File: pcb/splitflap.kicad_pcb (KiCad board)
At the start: 2 copper layers, 100 x 100 mm, 88 parts, among them J1 Motor D, J10 Hall C, J11 Hall B, J12 I2C, J2 Motor C, J3 Motor B, J4 Motor A, J5 BarrelJack Vertical, J6 USB_C_Receptacle_USB2.0_16P, J7 BarrelJack Horizontal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

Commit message: Add logo to the PCB
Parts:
- added G***: LOGO, LOGO, F.Cu at (109.8, 103.1)
- added G***: LOGO, LOGO, B.Cu at (143.4, 96.2)
- moved OSHW1 78.5 mm to (109.8, 71.8)
- moved R6 0.40 mm to (135.4, 145.0)

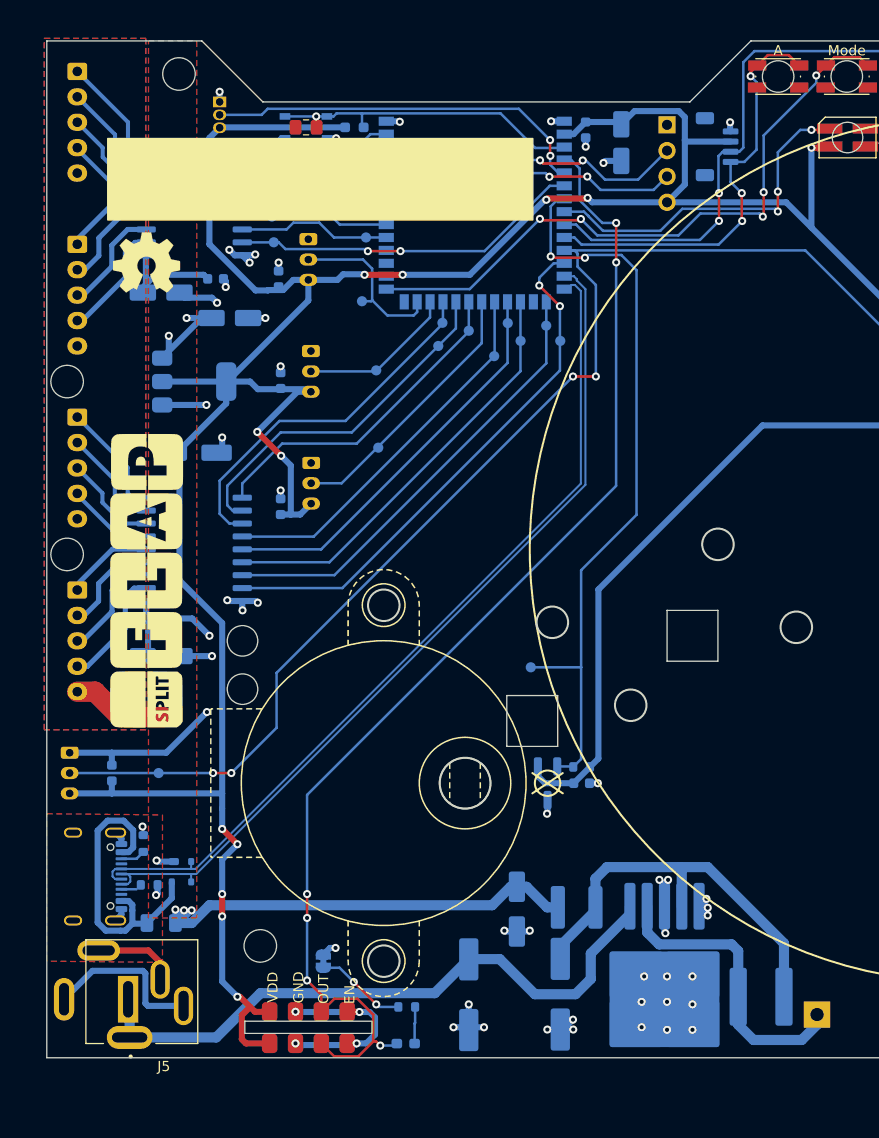
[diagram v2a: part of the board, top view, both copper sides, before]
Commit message: Silkscreen: Logo / Date / Commit Placeholder / Labels / PCB Way logo
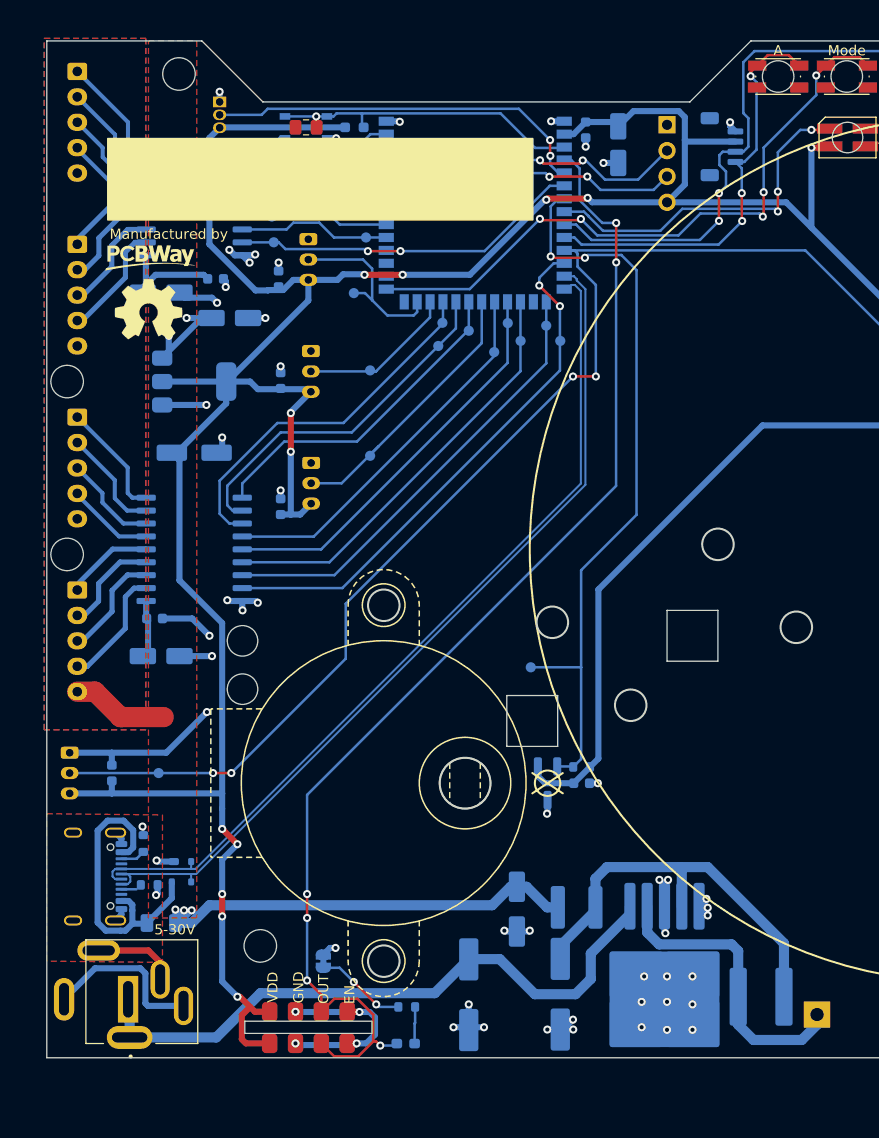
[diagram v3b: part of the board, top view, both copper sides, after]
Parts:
- G***: value LOGO -> Manufactured by
- J8, U5: value Hall A1 -> Hall Internal
- U9: value Hall A2 -> Hall Internal2
- moved G*** 32.1 mm to (110.2, 71.0), turned to 0 degrees
- moved OSHW1 4.60 mm to (110.0, 76.4)
- moved TP21 1.13 mm to (130.2, 74.8)
- moved TP19 1.13 mm to (131.8, 90.8)
- moved TP20 0.60 mm to (131.8, 82.4)
- moved J12 0.47 mm to (166.4, 60.4)
- moved TP8 0.40 mm to (144.0, 80.6)
- moved C16 0.36 mm to (156.2, 60.2)
- moved TP16 0.12 mm to (129.8, 60.9)
- turned G*** to -90 degrees
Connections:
- net /HALL_A2 renamed /HALL_INTERNAL2
- J8 pad 2: /HALL_A1 -> /HALL_INTERNAL
- R7 pad 2: /HALL_A1 -> /HALL_Internal
- TP17 pad 1: /HALL_A1 -> /HALL_INTERNAL
- U4 pad 11: /HALL_A1 -> /HALL_INTERNAL
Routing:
- net /HALL_A1: track 133.7 -> 0.00 mm, vias 6 -> 0
- net (no net): track 0.00 -> 133.7 mm
- net +3V3: track 360.5 -> 357.6 mm
- net /SWB_SDA: track 55.2 -> 56.3 mm
- net /HALL_D: track 17.0 -> 18.0 mm
- net /HALL_B: track 26.8 -> 27.8 mm
- net /SWA_SCL: track 41.8 -> 41.2 mm
- net /HALL_C: track 15.6 -> 16.1 mm
- net /HALL_INTERNAL: vias 0 -> 6
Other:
- board text added: "- < > +"
- board text added: "v2.0 @abcdef Designed in Switzerland Besmer Labs 24.03.2025 github.com/besi/split-flap-clock"

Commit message: Add Pinout
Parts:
- added G***: LOGO, LOGO, F.Cu at (114.2, 88.4)
- moved OSHW1 1.51 mm to (111.5, 76.6)
- moved G*** 0.73 mm to (110.9, 71.2)
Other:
- outline, holes or cut-outs redrawn
- board text added: "#279"
- board text added: "Pinout - Hall A: 10 9 3 8 - 18 (7) B: 13 14 21 11 - 12 C: 40 39 38 6 - 47 D: 1 2 42 41 - 48 DCF77: 4 SDA / SWB: 16 SCL / SWA: 17 Mode: 0 Neopixel: 15 Temp: 5"

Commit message: Fix HALL_INTERNAL label
The layout is not affected
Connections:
- R7 pad 2: /HALL_Internal -> /HALL_INTERNAL
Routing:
- net /HALL_INTERNAL: track 0.00 -> 133.7 mm
- net (no net): track 133.7 -> 0.00 mm
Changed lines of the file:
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@@
 	(net 67 "VBUS")
 	(net 68 "Net-(U5-OUTPUT)")
-	(net 69 "/HALL_Internal")
-	(net 70 "/HALL_INTERNAL")
+	(net 69 "/HALL_INTERNAL")
 	(footprint "Button_Switch_SMD:SW_Push_1P1T_NO_Vertical_Wuerth_434133025816"
 		(layer "F.Cu")
@@
 			(layers "*.Cu" "*.Mask")
 			(remove_unused_layers no)
-			(net 70 "/HALL_INTERNAL")
+			(net 69 "/HALL_INTERNAL")
 			(pinfunction "Pin_2")
 			(pintype "passive")
@@
 			(size 1.5 0.9)
 			(layers "B.Cu" "B.Paste" "B.Mask")
-			(net 70 "/HALL_INTERNAL")
+			(net 69 "/HALL_INTERNAL")
 			(pinfunction "IO18")
 			(pintype "bidirectional")
@@
 			(size 1 1)
 			(layers "B.Cu" "B.Mask")
-			(net 70 "/HALL_INTERNAL")
+			(net 69 "/HALL_INTERNAL")
 			(pinfunction "1")
 			(pintype "passive")
@@
 			(layers "B.Cu" "B.Paste" "B.Mask")
 			(roundrect_rratio 0.25)
-			(net 69 "/HALL_Internal")
+			(net 69 "/HALL_INTERNAL")
 			(pintype "passive")
 		)
@@
 	)
 	(segment
-		(start 151.749994 83)
-		(end 154 83)
-		(width 0.25)
-		(layer "F.Cu")
-		(net 0)
-	)
-	(segment
-		(start 189.9 83.749998)
-		(end 188.1 83.749998)
-		(width 0.25)
-		(layer "F.Cu")
-		(net 0)
-	)
-	(segment
-		(start 118.15 122)
-		(end 116.35 122)
-		(width 0.25)
-		(layer "F.Cu")
-		(net 0)
-	)
-	(segment
-		(start 174.6 70.6)
-		(end 150.89 70.6)
-		(width 0.25)
-		(layer "B.Cu")
-		(net 0)
-	)
-	(segment
-		(start 129.4 105.349994)
-		(end 151.749994 83)
-		(width 0.25)
-		(layer "B.Cu")
-		(net 0)
-	)
-	(segment
-		(start 116.35 122)
-		(end 102.25 122)
-		(width 0.25)
-		(layer "B.Cu")
-		(net 0)
-	)
-	(segment
-		(start 187.75 83.75)
-		(end 174.6 70.6)
-		(width 0.25)
-		(layer "B.Cu")
-		(net 0)
-	)
-	(segment
-		(start 192.6 85.2)
-		(end 192.6 85.775)
-		(width 0.25)
-		(layer "B.Cu")
-		(net 0)
-	)
-	(segment
-		(start 189.851578 83.750004)
-		(end 189.899994 83.750004)
-		(width 0.25)
-		(layer "B.Cu")
-		(net 0)
-	)
-	(segment
-		(start 154 83)
-		(end 154 74)
-		(width 0.25)
-		(layer "B.Cu")
-		(net 0)
-	)
-	(segment
-		(start 191.149998 83.749998)
-		(end 192.6 85.2)
-		(width 0.25)
-		(layer "B.Cu")
-		(net 0)
-	)
-	(segment
-		(start 188.1 83.749998)
-		(end 188.099998 83.75)
-		(width 0.25)
-		(layer "B.Cu")
-		(net 0)
-	)
-	(segment
-		(start 189.899994 83.750004)
-		(end 189.9 83.749998)
-		(width 0.25)
-		(layer "B.Cu")
-		(net 0)
-	)
-	(segment
-		(start 188.099998 83.75)
-		(end 187.75 83.75)
-		(width 0.25)
-		(layer "B.Cu")
-		(net 0)
-	)
-	(segment
-		(start 189.9 83.749998)
-		(end 191.149998 83.749998)
-		(width 0.25)
-		(layer "B.Cu")
-		(net 0)
-	)
-	(segment
-		(start 129.4 110.75)
-		(end 129.4 105.349994)
-		(width 0.25)
-		(layer "B.Cu")
-		(net 0)
-	)
-	(segment
-		(start 151.89 70.6)
-		(end 150.89 70.6)
-		(width 0.25)
-		(layer "B.Cu")
-		(net 0)
-	)
-	(segment
-		(start 154 74)
-		(end 152.2 72.2)
-		(width 0.25)
-		(layer "B.Cu")
-		(net 0)
-	)
-	(segment
-		(start 118.15 122)
-		(end 129.4 110.75)
-		(width 0.25)
-		(layer "B.Cu")
-		(net 0)
-	)
-	(segment
-		(start 152.2 70.91)
-		(end 151.89 70.6)
-		(width 0.25)
-		(layer "B.Cu")
-		(net 0)
-	)
-	(segment
-		(start 152.2 72.2)
-		(end 152.2 70.91)
-		(width 0.25)
-		(layer "B.Cu")
-		(net 0)
-	)
-	(segment
 		(start 107.25 116.5)
 		(end 111.5 116.5)
@@
 		(net 68)
 	)
+	(segment
+		(start 151.749994 83)
+		(end 154 83)
+		(width 0.25)
+		(layer "F.Cu")
+		(net 69)
+	)
+	(segment
+		(start 189.9 83.749998)
+		(end 188.1 83.749998)
+		(width 0.25)
+		(layer "F.Cu")
+		(net 69)
+	)
+	(segment
+		(start 118.15 122)
+		(end 116.35 122)
+		(width 0.25)
+		(layer "F.Cu")
+		(net 69)
+	)
 	(via
 		(at 118.15 122)
@@
 		(drill 0.4)
 		(layers "F.Cu" "B.Cu")
-		(net 70)
+		(net 69)
 	)
 	(via
@@
 		(drill 0.4)
 		(layers "F.Cu" "B.Cu")
-		(net 70)
+		(net 69)
 	)
 	(via
@@
 		(drill 0.4)
 		(layers "F.Cu" "B.Cu")
-		(net 70)
+		(net 69)
 	)
 	(via
@@
 		(drill 0.4)
 		(layers "F.Cu" "B.Cu")
-		(net 70)
+		(net 69)
 	)
 	(via
@@
 		(drill 0.4)
 		(layers "F.Cu" "B.Cu")
-		(net 70)
+		(net 69)
 	)
 	(via
@@
 		(drill 0.4)
 		(layers "F.Cu" "B.Cu")
-		(net 70)
+		(net 69)
+	)
+	(segment
+		(start 174.6 70.6)
+		(end 150.89 70.6)
+		(width 0.25)
+		(layer "B.Cu")
+		(net 69)
+	)
+	(segment
+		(start 129.4 105.349994)
+		(end 151.749994 83)
+		(width 0.25)
+		(layer "B.Cu")
+		(net 69)
+	)
+	(segment
+		(start 116.35 122)
+		(end 102.25 122)
+		(width 0.25)
+		(layer "B.Cu")
+		(net 69)
+	)
+	(segment
+		(start 187.75 83.75)
+		(end 174.6 70.6)
+		(width 0.25)
+		(layer "B.Cu")
+		(net 69)
+	)
+	(segment
+		(start 192.6 85.2)
+		(end 192.6 85.775)
+		(width 0.25)
+		(layer "B.Cu")
+		(net 69)
+	)
+	(segment
+		(start 189.851578 83.750004)
+		(end 189.899994 83.750004)
+		(width 0.25)
+		(layer "B.Cu")
+		(net 69)
+	)
+	(segment
+		(start 154 83)
+		(end 154 74)
+		(width 0.25)
+		(layer "B.Cu")
+		(net 69)
+	)
+	(segment
+		(start 191.149998 83.749998)
+		(end 192.6 85.2)
+		(width 0.25)
+		(layer "B.Cu")
+		(net 69)
+	)
+	(segment
+		(start 188.1 83.749998)
+		(end 188.099998 83.75)
+		(width 0.25)
+		(layer "B.Cu")
+		(net 69)
+	)
+	(segment
+		(start 189.899994 83.750004)
+		(end 189.9 83.749998)
+		(width 0.25)
+		(layer "B.Cu")
+		(net 69)
+	)
+	(segment
+		(start 188.099998 83.75)
+		(end 187.75 83.75)
+		(width 0.25)
+		(layer "B.Cu")
+		(net 69)
+	)
+	(segment
+		(start 189.9 83.749998)
+		(end 191.149998 83.749998)
+		(width 0.25)
+		(layer "B.Cu")
+		(net 69)
+	)
+	(segment
+		(start 129.4 110.75)
+		(end 129.4 105.349994)
+		(width 0.25)
+		(layer "B.Cu")
+		(net 69)
+	)
+	(segment
+		(start 151.89 70.6)
+		(end 150.89 70.6)
+		(width 0.25)
+		(layer "B.Cu")
+		(net 69)
+	)
+	(segment
+		(start 154 74)
+		(end 152.2 72.2)
+		(width 0.25)
+		(layer "B.Cu")
+		(net 69)
+	)
+	(segment
+		(start 118.15 122)
+		(end 129.4 110.75)
+		(width 0.25)
+		(layer "B.Cu")
+		(net 69)
+	)
+	(segment
+		(start 152.2 70.91)
+		(end 151.89 70.6)
+		(width 0.25)
+		(layer "B.Cu")
+		(net 69)
+	)
+	(segment
+		(start 152.2 72.2)
+		(end 152.2 70.91)
+		(width 0.25)
+		(layer "B.Cu")
+		(net 69)
 	)
 	(zone

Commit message: Cleanup schematics
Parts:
- J6: value USB_C_Receptacle_USB2.0_16P -> USB-C Plug
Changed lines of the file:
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@@
 			)
 		)
-		(property "Value" "USB_C_Receptacle_USB2.0_16P"
+		(property "Value" "USB-C Plug"
 			(at 0 -5 -90)
 			(unlocked yes)

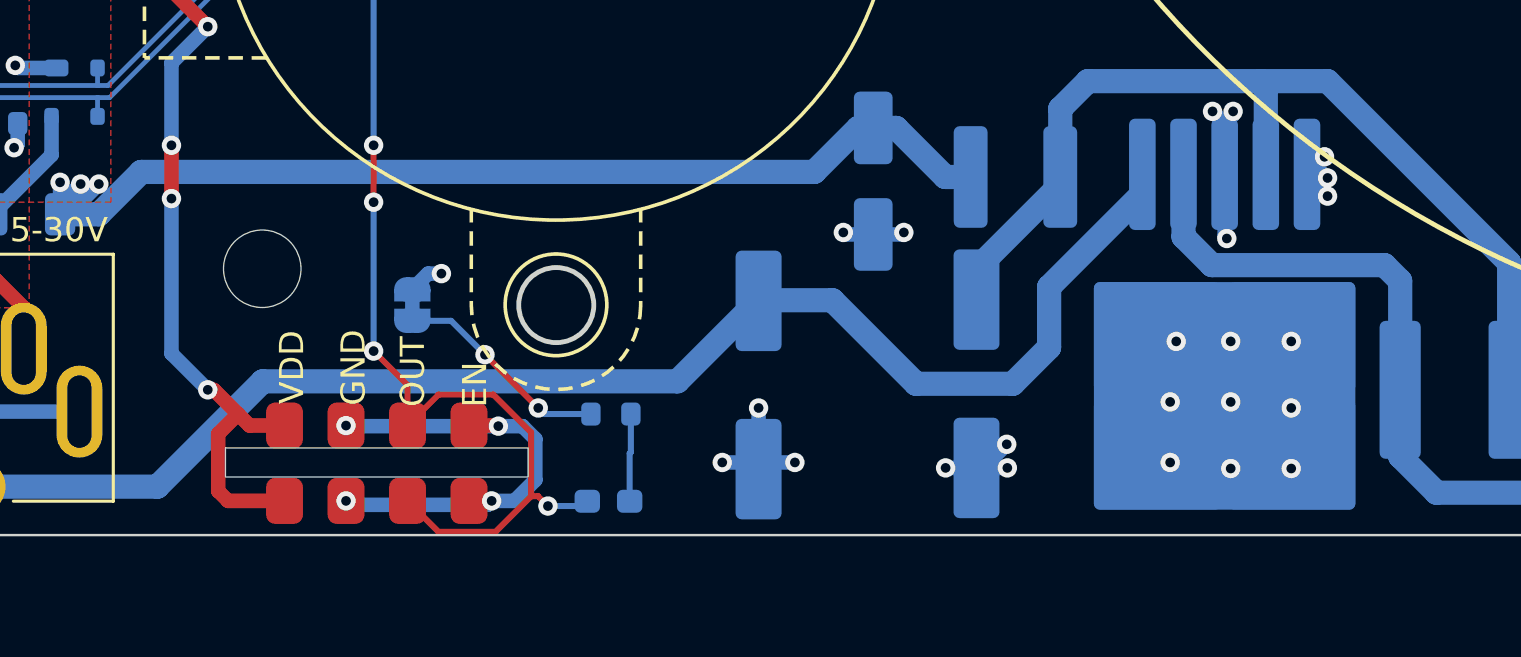
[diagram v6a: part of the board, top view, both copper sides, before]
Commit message: Move vias out of the pads
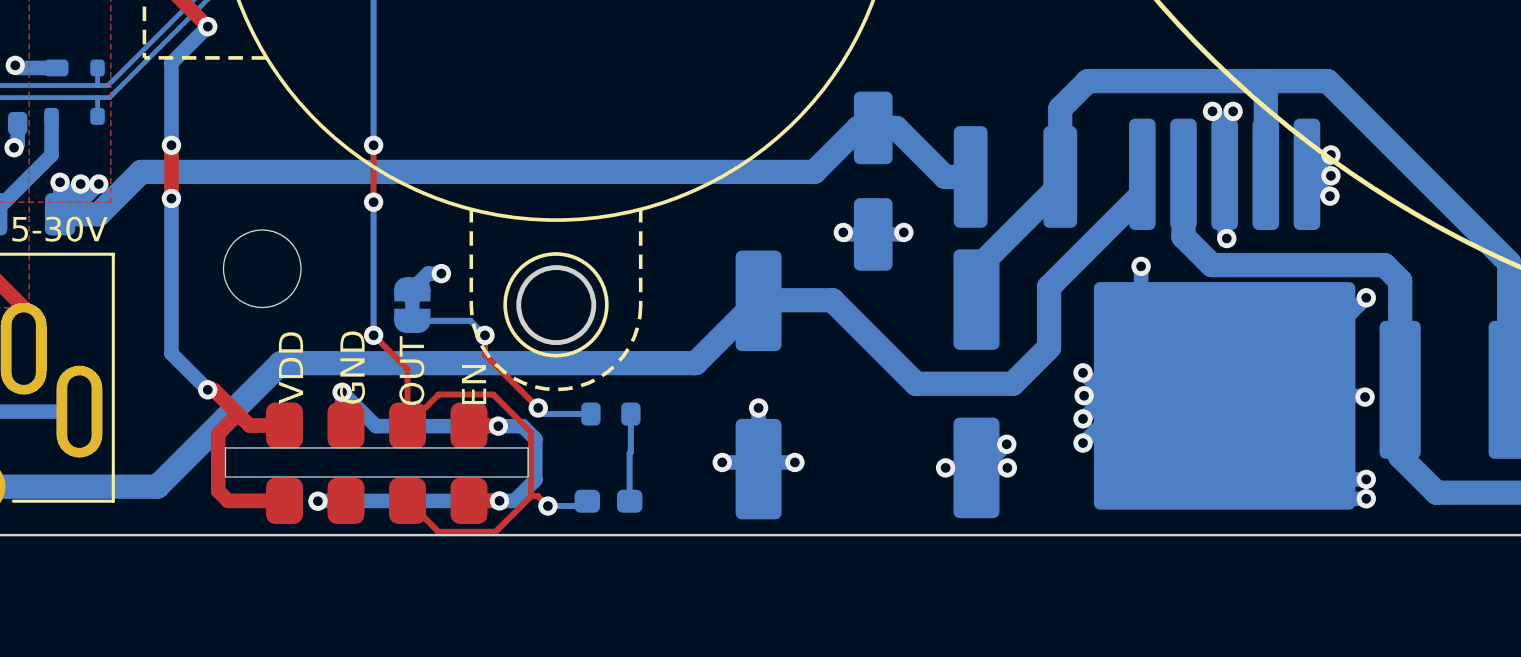
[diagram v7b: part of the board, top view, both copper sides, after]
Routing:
- net GND: track 121.4 -> 180.5 mm

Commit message: Correlate footprints according to the feedback from the Fab-house
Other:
- board text added: "v2.0 @3d2c2404 Designed in Switzerland Besmer Labs 25.03.2025 github.com/besi/split-flap-clock"
- board text removed: "v2.0 @abcdef Designed in Switzerland Besmer Labs 24.03.2025 github.com/besi/split-flap-clock"
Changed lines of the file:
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@@
 			)
 		)
-		(property "MPN" "CP-060A-ND"
+		(property "MPN" "PJ-060A"
 			(at 0 0 180)
 			(unlocked yes)
@@
 		)
 		(model "${KICAD8_3DMODEL_DIR}/Inductor_SMD.3dshapes/L_APV_ANR5045.wrl"
+			(hide yes)
 			(offset
 				(xyz 0 0 0)
@@
 			)
 		)
+		(model "${KIPRJMOD}/lib/TYS5040220M-10.step"
+			(offset
+				(xyz 0 3 0)
+			)
+			(scale
+				(xyz 1 1 1)
+			)
+			(rotate
+				(xyz 0 0 0)
+			)
+		)
 	)
 	(footprint "TestPoint:TestPoint_Pad_D1.0mm"
@@
 		(layer "F.Fab")
 	)
-	(gr_text "v2.0 @abcdef\nDesigned in Switzerland \nBesmer Labs 24.03.2025\ngithub.com/besi/split-flap-clock"
+	(gr_text "v2.0 @3d2c2404\nDesigned in Switzerland \nBesmer Labs 25.03.2025\ngithub.com/besi/split-flap-clock"
 		(at 139 81.8 90)
 		(layer "B.SilkS")
